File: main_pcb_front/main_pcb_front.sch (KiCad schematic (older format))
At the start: 10 parts

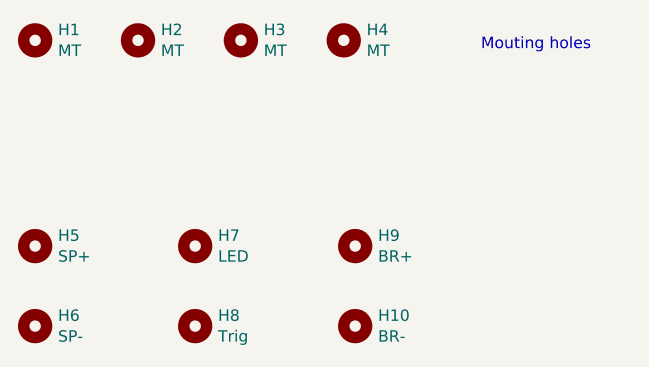
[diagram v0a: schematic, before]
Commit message: Added power button and its protector to the front pcb
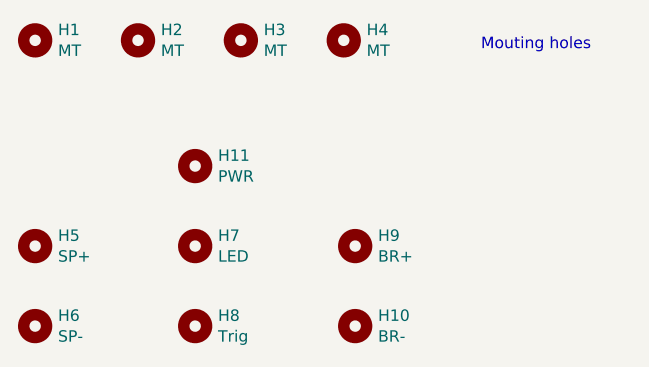
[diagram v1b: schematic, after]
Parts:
- added H11: PWR, main_pcb_front:MountingHole_PowerBtn, symbol Mechanical:MountingHole
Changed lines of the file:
@@
+	1    0    0    -1
+$EndComp
+$Comp
+L Mechanical:MountingHole H11
+U 1 1 617D3C5C
+P 4750 2550
+F 0 "H11" H 4850 2596 50  0000 L CNN
+F 1 "PWR" H 4850 2505 50  0000 L CNN
+F 2 "main_pcb_front:MountingHole_PowerBtn" H 4750 2550 50  0001 C CNN
+F 3 "~" H 4750 2550 50  0001 C CNN
+	1    4750 2550
 	1    0    0    -1
 $EndComp

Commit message: Increased front panel PCB holes for buttons to 4mm
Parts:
- H10, H5, H6, H7, H8, H9: footprint MountingHole:MountingHole_3.2mm_M3 -> MountingHole:MountingHole_4.3mm_M4
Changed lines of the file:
@@
 F 0 "H7" H 4850 2946 50  0000 L CNN
 F 1 "LED" H 4850 2855 50  0000 L CNN
-F 2 "MountingHole:MountingHole_3.2mm_M3" H 4750 2900 50  0001 C CNN
+F 2 "MountingHole:MountingHole_4.3mm_M4" H 4750 2900 50  0001 C CNN
 F 3 "~" H 4750 2900 50  0001 C CNN
 	1    4750 2900
@@
 F 0 "H5" H 4150 2946 50  0000 L CNN
 F 1 "SP+" H 4150 2855 50  0000 L CNN
-F 2 "MountingHole:MountingHole_3.2mm_M3" H 4050 2900 50  0001 C CNN
+F 2 "MountingHole:MountingHole_4.3mm_M4" H 4050 2900 50  0001 C CNN
 F 3 "~" H 4050 2900 50  0001 C CNN
 	1    4050 2900
@@
 F 0 "H6" H 4150 3296 50  0000 L CNN
 F 1 "SP-" H 4150 3205 50  0000 L CNN
-F 2 "MountingHole:MountingHole_3.2mm_M3" H 4050 3250 50  0001 C CNN
+F 2 "MountingHole:MountingHole_4.3mm_M4" H 4050 3250 50  0001 C CNN
 F 3 "~" H 4050 3250 50  0001 C CNN
 	1    4050 3250
@@
 F 0 "H8" H 4850 3296 50  0000 L CNN
 F 1 "Trig" H 4850 3205 50  0000 L CNN
-F 2 "MountingHole:MountingHole_3.2mm_M3" H 4750 3250 50  0001 C CNN
+F 2 "MountingHole:MountingHole_4.3mm_M4" H 4750 3250 50  0001 C CNN
 F 3 "~" H 4750 3250 50  0001 C CNN
 	1    4750 3250
@@
 F 0 "H9" H 5550 2946 50  0000 L CNN
 F 1 "BR+" H 5550 2855 50  0000 L CNN
-F 2 "MountingHole:MountingHole_3.2mm_M3" H 5450 2900 50  0001 C CNN
+F 2 "MountingHole:MountingHole_4.3mm_M4" H 5450 2900 50  0001 C CNN
 F 3 "~" H 5450 2900 50  0001 C CNN
 	1    5450 2900
@@
 F 0 "H10" H 5550 3296 50  0000 L CNN
 F 1 "BR-" H 5550 3205 50  0000 L CNN
-F 2 "MountingHole:MountingHole_3.2mm_M3" H 5450 3250 50  0001 C CNN
+F 2 "MountingHole:MountingHole_4.3mm_M4" H 5450 3250 50  0001 C CNN
 F 3 "~" H 5450 3250 50  0001 C CNN
 	1    5450 3250
